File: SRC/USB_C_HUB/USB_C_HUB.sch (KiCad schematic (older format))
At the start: 38 parts

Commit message: PD controller_ power components inclusion pending
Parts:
- removed C? (x3): 10uF, symbol Device:C_Small
- removed C? (x2): 47uF, symbol Device:C_Small
- removed C?: 1uF, symbol Device:C_Small
- removed C?: 0.01uF, symbol Device:C_Small
- removed C? (x2): 22uF, symbol Device:C_Small
- removed C? (x2): 220pF, symbol Device:C_Small
- removed C? (x3): 0.1uF, symbol Device:C_Small
- removed D?: D_Schottky, symbol Device:D_Schottky
- removed D?: D12V0L1B2LP-7B, Diode_SMD:D_01005_0402Metric, symbol dk_TVS-Diodes:PGB1010603MR
- removed J?: USB_C_Receptacle, symbol Connector:USB_C_Receptacle
- removed Q? (x2): SI7997DP, symbol usb_hub:SI7997DP
- removed Q? (x2): MMBF2201NT1G, digikey-footprints:SOT-323, symbol dk_Transistors-FETs-MOSFETs-Single:2N7002P_215
- removed R?: 10K_603, symbol Device:R_US
- removed R?: 30K_603, symbol Device:R_US
- removed R?: 20K_603, symbol Device:R_US
- removed R?: 5K_805, symbol Device:R_US
- removed R?: 100K, symbol Device:R_US
- removed R? (x6): 10K, symbol Device:R_US
- removed R?: 576K, symbol Device:R_US
- removed R? (x2): 1K, symbol Device:R_US
- removed U?: TPS65987D, symbol usb_hub:TPS65987D
- removed U?: TLV1701AIDBVR, Package_TO_SOT_SMD:SOT-23-5, symbol Amplifier_Operational:TLV172IDCK
- removed Z?: BZT52C11-7-F, digikey-footprints:SOD-123, symbol dk_Diodes-Zener-Single:MMSZ5231B-7-F
- added P?: USB_C_Plug, symbol Connector:USB_C_Plug
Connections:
- net labels added: VCONN
- net labels removed: +3.3V, +5V, ADCIN1, ADCIN2, COMP_IN, COMP_OUT, C_CC2, GND_FET, LDO_3V3, POWER_IN(PP_EXT1), PP_EXT_CNTRL
- wire segments 198 -> 13
- no-connect marks 12 -> 0
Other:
- note added: "Connected to computer(host).\n"
- note added: "UPWARD FACING PORT(UFP)\n"
- note removed: "BP_WaitFor3V3_Internal mode\ndiv=0.25, SPI_POCI=1\nR1=30K, R2=10K."
- note removed: "CHARGER INPUT\nTYPE C\nRECEPTACLE"
- note removed: "GND_NMOS comes from the \ncomparator. When no power is \npressent the comparator connectes the \nPP_EXT_CNTRL pin to GND via NMOS"
- note removed: "PP_EXT_CNTRL turns on the mosfet via \na gate thus making the PP_EXT1 mosfet\ngate zero. turning on the mosfet and\n allowing current flow"
- note removed: "The TPS65987D requires firmware \nprogramming via a downloadable GUI tool.\nRecomendation: Since the system takes in a \ncharger we can configure it as a Source device\n(read:https://www.embedded.com/usb-type-c-and-power-delivery-101-ports-and-connections/) \nSecondly: we can configure it as a DRP device that can source(provide) or sink(receive) power. Its a source when the charging \nreceptacle 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"
- note removed: "UNUSED \nIN THE TYPE C \nCHARGING INPUT"
- note removed: "VOLTAGE COMPARATOR"
- note removed: "sets the I2C address\nDIV = R2/(R1+R2)\nR1=5K, R2=20K\nDIV=0.8, ADD=011b"

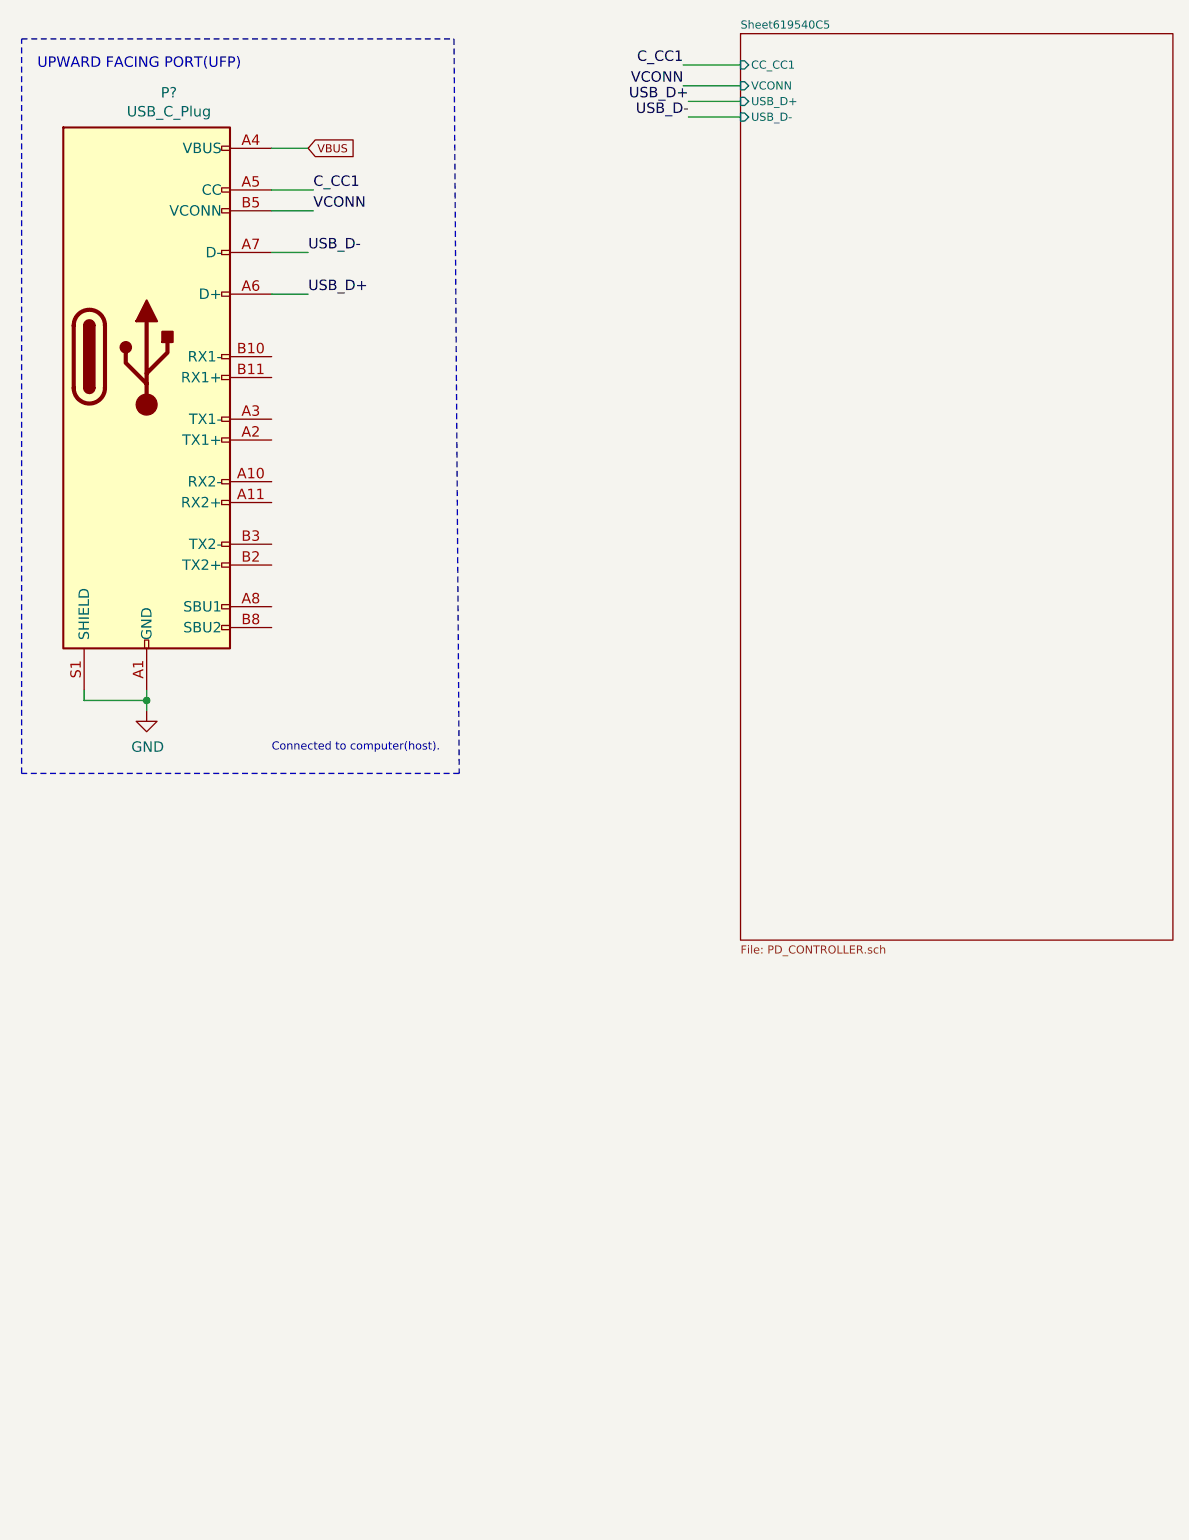
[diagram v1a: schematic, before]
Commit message: PD controller + variable voltage source input(will handle voltage requestvia PD)
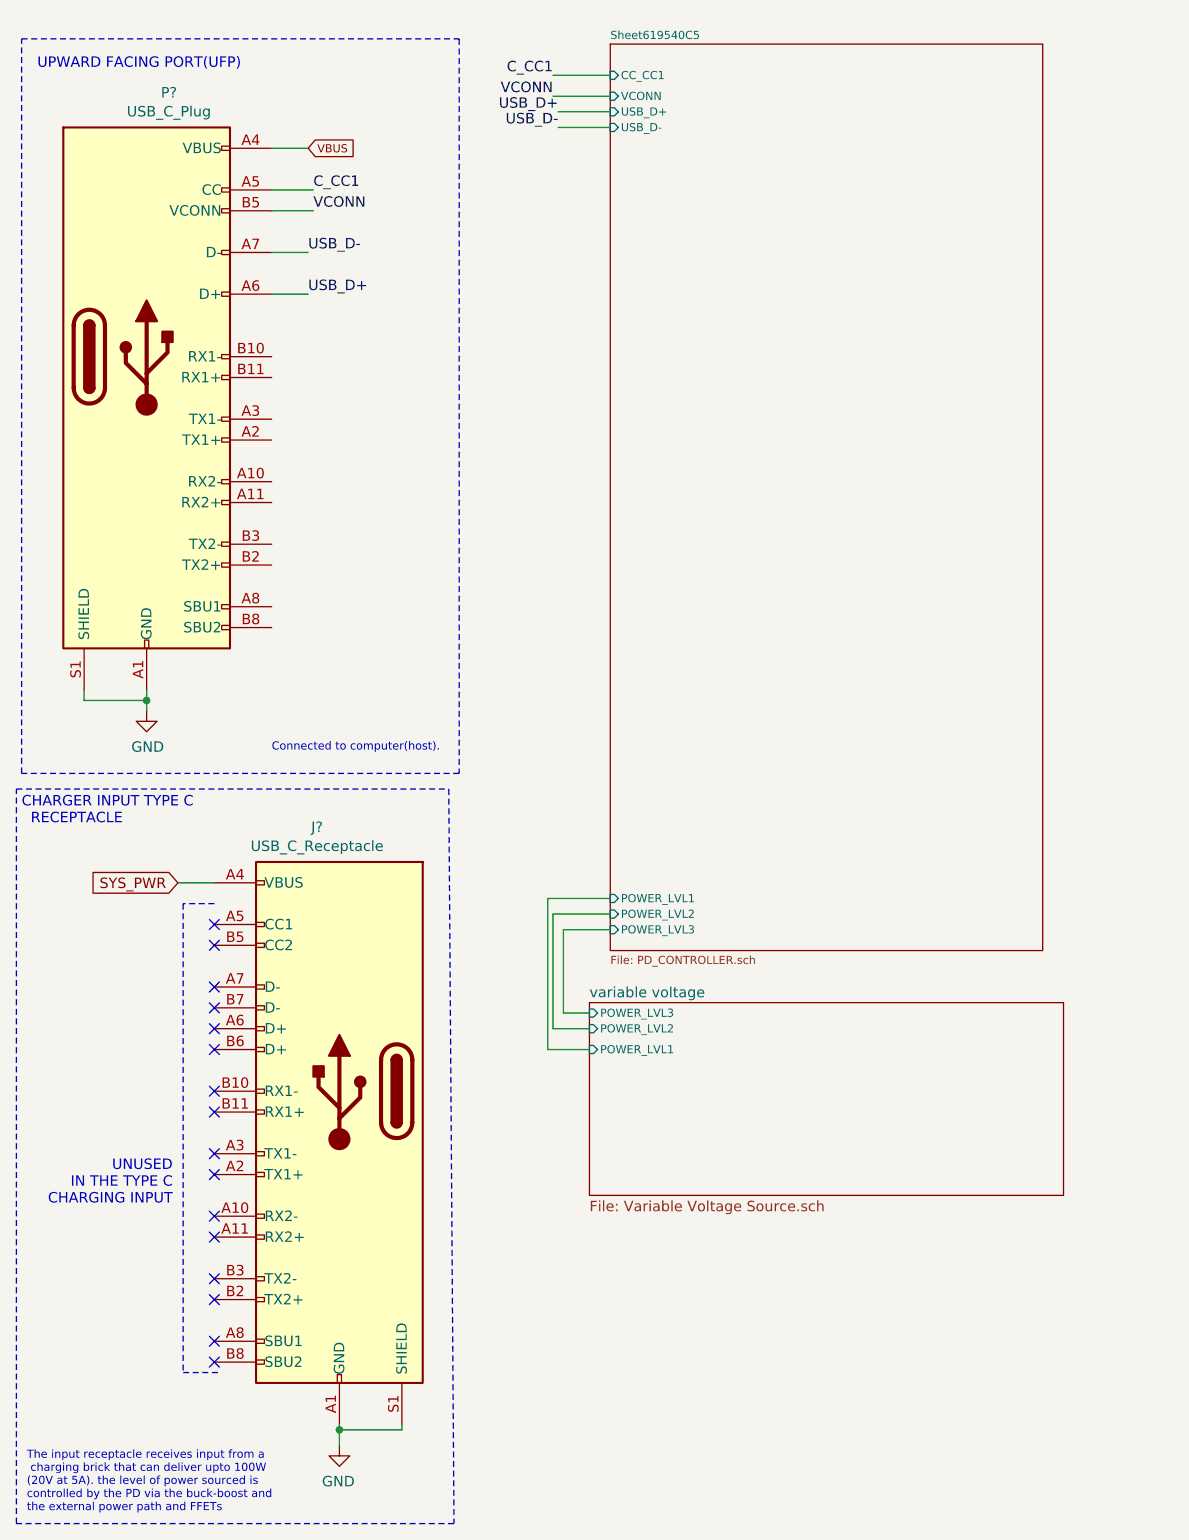
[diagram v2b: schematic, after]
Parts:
- added J?: USB_C_Receptacle, symbol Connector:USB_C_Receptacle
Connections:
- net GND: now also J?.A1 (GND), J?.A12 (GND), J?.B1 (GND), J?.B12 (GND), J?.S1 (SHIELD)
- new net SYS_PWR: J?.A4 (VBUS), J?.A9 (VBUS), J?.B4 (VBUS), J?.B9 (VBUS)
- no-connect marks 0 -> 16
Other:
- note added: "CHARGER INPUT TYPE C\n RECEPTACLE"
- note added: "The input receptacle receives input from a\n charging brick that can deliver upto 100W\n(20V at 5A). the level of power sourced is \ncontrolled by the PD via the buck-boost and \nthe external power path and FFETs"
- note added: "UNUSED \nIN THE TYPE C \nCHARGING INPUT"
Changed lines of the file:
@@
 $Descr A4 11693 8268
 encoding utf-8
-Sheet 1 2
+Sheet 1 3
 Title ""
 Date ""
@@
 	1750 1125 1925 1125
 Wire Notes Line
-	2625 600  2650 4125
+	2650 600  2650 4125
 Wire Notes Line
 	2650 4125 550  4125
@@
 	550  4125 550  600
 Wire Notes Line
-	550  600  2625 600
+	550  600  2650 600
 Wire Wire Line
 	1750 1825 1925 1825
@@
 Text GLabel 1925 1125 2    39   Input ~ 0
 VBUS
-Text Label 3725 725  2    50   ~ 0
+Text Label 3100 775  2    50   ~ 0
 C_CC1
-Text Label 3725 825  2    50   ~ 0
+Text Label 3100 875  2    50   ~ 0
 VCONN
 Wire Wire Line
-	3725 725  4000 725
-Wire Wire Line
-	3725 825  4000 825
-Text Label 3750 900  2    50   ~ 0
+	3100 775  3375 775
+Wire Wire Line
+	3100 875  3375 875
+Text Label 3125 950  2    50   ~ 0
 USB_D+
-Text Label 3750 975  2    50   ~ 0
+Text Label 3125 1025 2    50   ~ 0
 USB_D-
 $Sheet
-S 4000 575  2075 4350
+S 3375 625  2075 4350
 U 619540C6
 F0 "Sheet619540C5" 39
 F1 "PD_CONTROLLER.sch" 39
-F2 "CC_CC1" I L 4000 725 39
-F3 "VCONN" I L 4000 825 39
-F4 "USB_D+" I L 4000 900 39
-F5 "USB_D-" I L 4000 975 39
+F2 "CC_CC1" I L 3375 775 39
+F3 "VCONN" I L 3375 875 39
+F4 "USB_D+" I L 3375 950 39
+F5 "USB_D-" I L 3375 1025 39
+F6 "POWER_LVL1" I L 3375 4725 39
+F7 "POWER_LVL2" I L 3375 4800 39
+F8 "POWER_LVL3" I L 3375 4875 39
 $EndSheet
 Wire Wire Line
-	4000 900  3750 900
-Wire Wire Line
-	3750 975  4000 975
+	3375 950  3125 950
+Wire Wire Line
+	3125 1025 3375 1025
+Wire Notes Line
+	2600 4200 2625 7725
+Wire Wire Line
+	2075 7275 2075 7350
+Connection ~ 2075 7275
+Wire Wire Line
+	2375 7275 2075 7275
+Wire Wire Line
+	2375 7250 2375 7275
+NoConn ~ 1475 4950
+NoConn ~ 1475 4850
+Wire Notes Line
+	525  4200 2600 4200
+Wire Notes Line
+	525  7725 525  4200
+Wire Notes Line
+	2625 7725 525  7725
+Wire Wire Line
+	1475 4650 1300 4650
+Wire Wire Line
+	2075 7250 2075 7275
+$Comp
+L OLIMEX_Power:GND #PWR?
+U 1 1 61C31561
+P 2075 7350
+AR Path="/619540C6/61C31561" Ref="#PWR?"  Part="1"
+AR Path="/61C31561" Ref="#PWR?"  Part="1"
+F 0 "#PWR?" H 2075 7100 50  0001 C CNN
+F 1 "GND" H 2080 7177 50  0000 C CNN
+F 2 "" H 2075 7350 60  0000 C CNN
+F 3 "" H 2075 7350 60  0000 C CNN
+	1    2075 7350
+	-1   0    0    -1
+$EndComp
+Text Notes 1275 6200 2    50   ~ 0
+UNUSED \nIN THE TYPE C \nCHARGING INPUT
+Wire Notes Line
+	1325 7000 1500 7000
+Wire Notes Line
+	1325 4750 1325 7000
+Wire Notes Line
+	1475 4750 1325 4750
+NoConn ~ 1475 6950
+NoConn ~ 1475 6850
+NoConn ~ 1475 6650
+NoConn ~ 1475 6550
+NoConn ~ 1475 6350
+NoConn ~ 1475 6250
+NoConn ~ 1475 6050
+NoConn ~ 1475 5950
+NoConn ~ 1475 5750
+NoConn ~ 1475 5650
+Text Notes 550  4375 0    50   ~ 0
+CHARGER INPUT TYPE C\n  RECEPTACLE
+$Comp
+L Connector:USB_C_Receptacle J?
+U 1 1 61C31576
+P 2075 5650
+AR Path="/619540C6/61C31576" Ref="J?"  Part="1"
+AR Path="/61C31576" Ref="J?"  Part="1"
+F 0 "J?" H 2182 6917 50  0000 C CNN
+F 1 "USB_C_Receptacle" H 2182 6826 50  0000 C CNN
+F 2 "" H 2225 5650 50  0001 C CNN
+F 3 "https://www.usb.org/sites/default/files/documents/usb_type-c.zip" H 2225 5650 50  0001 C CNN
+	1    2075 5650
+	-1   0    0    -1
+$EndComp
+NoConn ~ 1475 5150
+NoConn ~ 1475 5250
+NoConn ~ 1475 5350
+NoConn ~ 1475 5450
+Text Notes 575  7675 0    39   ~ 0
+The input receptacle receives input from a\n charging brick that can deliver upto 100W\n(20V at 5A). the level of power sourced is \ncontrolled by the PD via the buck-boost and \nthe external power path and FFETs
+Text GLabel 1300 4650 0    50   Input ~ 0
+SYS_PWR
+$Sheet
+S 3275 5225 2275 925
+U 61C45066
+F0 "variable voltage" 50
+F1 "Variable Voltage Source.sch" 50
+F2 "POWER_LVL1" I L 3275 5450 39
+F3 "POWER_LVL2" I L 3275 5350 39
+F4 "POWER_LVL3" I L 3275 5275 39
+$EndSheet
+Wire Wire Line
+	3375 4725 3075 4725
+Wire Wire Line
+	3075 4725 3075 5450
+Wire Wire Line
+	3075 5450 3275 5450
+Wire Wire Line
+	3275 5350 3100 5350
+Wire Wire Line
+	3100 5350 3100 4800
+Wire Wire Line
+	3100 4800 3375 4800
+Wire Wire Line
+	3375 4875 3150 4875
+Wire Wire Line
+	3150 4875 3150 5275
+Wire Wire Line
+	3150 5275 3275 5275
 $EndSCHEMATC

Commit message: With ST PD controller(sink)100W
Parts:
- added D?: ESDA25P35, digikey-footprints:SOD-523, symbol dk_TVS-Diodes:ESD5Z3_3T1G
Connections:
- net CC1_PWR: now reaches J?.A5 (CC1)
- net CC2_PWR: now reaches J?.B5 (CC2)
- net SYS_PWR renamed PWR_IN
- no-connect marks 16 -> 14
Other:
- note added: "PRESERVED FOR USE LATER_\nNO CONNECTION TO THE SCHEMATIC"
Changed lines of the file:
@@
 Text GLabel 1925 1125 2    39   Input ~ 0
 VBUS
-Text Label 3100 775  2    50   ~ 0
-C_CC1
-Text Label 3100 875  2    50   ~ 0
-VCONN
-Wire Wire Line
-	3100 775  3375 775
-Wire Wire Line
-	3100 875  3375 875
-Text Label 3125 950  2    50   ~ 0
-USB_D+
-Text Label 3125 1025 2    50   ~ 0
-USB_D-
-$Sheet
-S 3375 625  2075 4350
-U 619540C6
-F0 "Sheet619540C5" 39
-F1 "PD_CONTROLLER.sch" 39
-F2 "CC_CC1" I L 3375 775 39
-F3 "VCONN" I L 3375 875 39
-F4 "USB_D+" I L 3375 950 39
-F5 "USB_D-" I L 3375 1025 39
-F6 "POWER_LVL1" I L 3375 4725 39
-F7 "POWER_LVL2" I L 3375 4800 39
-F8 "POWER_LVL3" I L 3375 4875 39
-$EndSheet
-Wire Wire Line
-	3375 950  3125 950
-Wire Wire Line
-	3125 1025 3375 1025
 Wire Notes Line
-	2600 4200 2625 7725
+	2650 4200 2650 7725
 Wire Wire Line
 	2075 7275 2075 7350
@@
 Wire Wire Line
 	2375 7250 2375 7275
-NoConn ~ 1475 4950
-NoConn ~ 1475 4850
 Wire Notes Line
-	525  4200 2600 4200
+	525  4200 2650 4200
 Wire Notes Line
 	525  7725 525  4200
 Wire Notes Line
-	2625 7725 525  7725
+	2650 7725 525  7725
 Wire Wire Line
 	1475 4650 1300 4650
@@
 	1325 7000 1500 7000
 Wire Notes Line
-	1325 4750 1325 7000
+	1325 5050 1325 7000
 Wire Notes Line
-	1475 4750 1325 4750
+	1525 5050 1325 5050
 NoConn ~ 1475 6950
 NoConn ~ 1475 6850
@@
 Text Notes 575  7675 0    39   ~ 0
 The input receptacle receives input from a\n charging brick that can deliver upto 100W\n(20V at 5A). the level of power sourced is \ncontrolled by the PD via the buck-boost and \nthe external power path and FFETs
-Text GLabel 1300 4650 0    50   Input ~ 0
-SYS_PWR
+Wire Wire Line
+	1475 4850 1300 4850
+Wire Wire Line
+	1475 4950 1300 4950
+Text Label 1300 4850 2    39   ~ 0
+CC1_PWR
+$Comp
+L dk_TVS-Diodes:ESD5Z3_3T1G D?
+U 1 1 61D69198
+P 1500 6900
+AR Path="/61C45066/61D69198" Ref="D?"  Part="1"
+AR Path="/61D69198" Ref="D?"  Part="1"
+F 0 "D?" V 1553 6772 60  0000 R CNN
+F 1 "ESDA25P35" V 1447 6772 60  0000 R CNN
+F 2 "digikey-footprints:SOD-523" H 1700 7100 60  0001 L CNN
+F 3 "https://www.onsemi.com/pub/Collateral/ESD5Z2.5T1-D.PDF" H 1700 7200 60  0001 L CNN
+F 4 "ESD5Z3.3T1GOSCT-ND" H 1700 7300 60  0001 L CNN "Digi-Key_PN"
+F 5 "ESD5Z3.3T1G" H 1700 7400 60  0001 L CNN "MPN"
+F 6 "Circuit Protection" H 1700 7500 60  0001 L CNN "Category"
+F 7 "TVS - Diodes" H 1700 7600 60  0001 L CNN "Family"
+F 8 "https://www.onsemi.com/pub/Collateral/ESD5Z2.5T1-D.PDF" H 1700 7700 60  0001 L CNN "DK_Datasheet_Link"
+F 9 "/product-detail/en/on-semiconductor/ESD5Z3.3T1G/ESD5Z3.3T1GOSCT-ND/1967044" H 1700 7800 60  0001 L CNN "DK_Detail_Page"
+F 10 "TVS DIODE 3.3V 14.1V SOD523" H 1700 7900 60  0001 L CNN "Description"
+F 11 "ON Semiconductor" H 1700 8000 60  0001 L CNN "Manufacturer"
+F 12 "Active" H 1700 8100 60  0001 L CNN "Status"
+	1    1500 6900
+	0    -1   -1   0
+$EndComp
+Text Label 1300 4950 2    39   ~ 0
+CC2_PWR
+Text Label 1300 4650 2    50   ~ 0
+PWR_IN
+Text Label 2950 4525 2    50   ~ 0
+PWR_IN
 $Sheet
-S 3275 5225 2275 925
-U 61C45066
-F0 "variable voltage" 50
-F1 "Variable Voltage Source.sch" 50
-F2 "POWER_LVL1" I L 3275 5450 39
-F3 "POWER_LVL2" I L 3275 5350 39
-F4 "POWER_LVL3" I L 3275 5275 39
+S 11775 6725 2525 1500
+U 61EF7DEC
+F0 "UFP_PD_CONTROLLER" 50
+F1 "UFP_PD_CTRL + VAR_V_SOURCE.sch" 50
 $EndSheet
+Text Notes 12150 7325 0    50   ~ 0
+PRESERVED FOR USE LATER_\nNO CONNECTION TO THE SCHEMATIC
 Wire Wire Line
-	3375 4725 3075 4725
-Wire Wire Line
-	3075 4725 3075 5450
-Wire Wire Line
-	3075 5450 3275 5450
-Wire Wire Line
-	3275 5350 3100 5350
-Wire Wire Line
-	3100 5350 3100 4800
-Wire Wire Line
-	3100 4800 3375 4800
-Wire Wire Line
-	3375 4875 3150 4875
-Wire Wire Line
-	3150 4875 3150 5275
-Wire Wire Line
-	3150 5275 3275 5275
+	3050 4525 2950 4525
+$Sheet
+S 3050 4425 2325 975
+U 61DDBD9F
+F0 "ST_PD CHARGING" 39
+F1 "ST_PD CHARGING CONTROLLER.sch" 39
+F2 "PWR_IN" I L 3050 4525 39
+$EndSheet
 $EndSCHEMATC

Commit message: With ST PD controller(sink)100W
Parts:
- removed D?: ESDA25P35, digikey-footprints:SOD-523, symbol dk_TVS-Diodes:ESD5Z3_3T1G
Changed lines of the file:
@@
 $Descr A4 11693 8268
 encoding utf-8
-Sheet 1 3
+Sheet 1 4
 Title ""
 Date ""
@@
 Text Label 1300 4850 2    39   ~ 0
 CC1_PWR
-$Comp
-L dk_TVS-Diodes:ESD5Z3_3T1G D?
-U 1 1 61D69198
-P 1500 6900
-AR Path="/61C45066/61D69198" Ref="D?"  Part="1"
-AR Path="/61D69198" Ref="D?"  Part="1"
-F 0 "D?" V 1553 6772 60  0000 R CNN
-F 1 "ESDA25P35" V 1447 6772 60  0000 R CNN
-F 2 "digikey-footprints:SOD-523" H 1700 7100 60  0001 L CNN
-F 3 "https://www.onsemi.com/pub/Collateral/ESD5Z2.5T1-D.PDF" H 1700 7200 60  0001 L CNN
-F 4 "ESD5Z3.3T1GOSCT-ND" H 1700 7300 60  0001 L CNN "Digi-Key_PN"
-F 5 "ESD5Z3.3T1G" H 1700 7400 60  0001 L CNN "MPN"
-F 6 "Circuit Protection" H 1700 7500 60  0001 L CNN "Category"
-F 7 "TVS - Diodes" H 1700 7600 60  0001 L CNN "Family"
-F 8 "https://www.onsemi.com/pub/Collateral/ESD5Z2.5T1-D.PDF" H 1700 7700 60  0001 L CNN "DK_Datasheet_Link"
-F 9 "/product-detail/en/on-semiconductor/ESD5Z3.3T1G/ESD5Z3.3T1GOSCT-ND/1967044" H 1700 7800 60  0001 L CNN "DK_Detail_Page"
-F 10 "TVS DIODE 3.3V 14.1V SOD523" H 1700 7900 60  0001 L CNN "Description"
-F 11 "ON Semiconductor" H 1700 8000 60  0001 L CNN "Manufacturer"
-F 12 "Active" H 1700 8100 60  0001 L CNN "Status"
-	1    1500 6900
-	0    -1   -1   0
-$EndComp
 Text Label 1300 4950 2    39   ~ 0
 CC2_PWR
@@
 F2 "PWR_IN" I L 3050 4525 39
 $EndSheet
+$Sheet
+S 3175 700  1675 1050
+U 61F5E4BA
+F0 "5V_BUCK" 50
+F1 "5V_BUCK.sch" 50
+$EndSheet
 $EndSCHEMATC

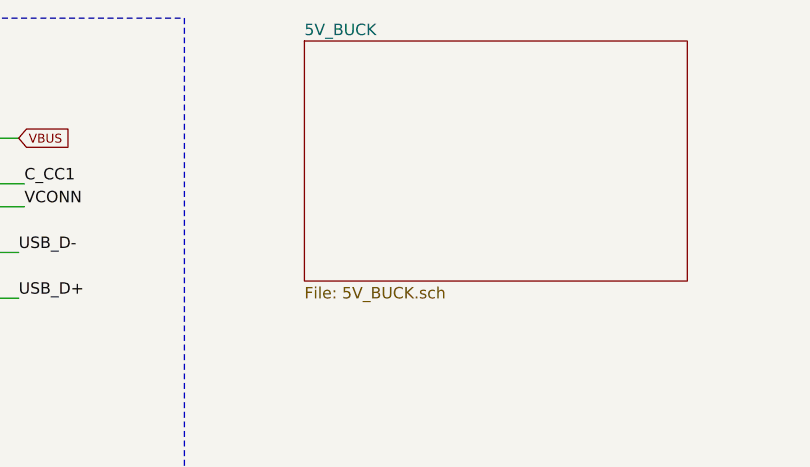
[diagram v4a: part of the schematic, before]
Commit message: With ST_PD controller, Buck $ Boost regulators
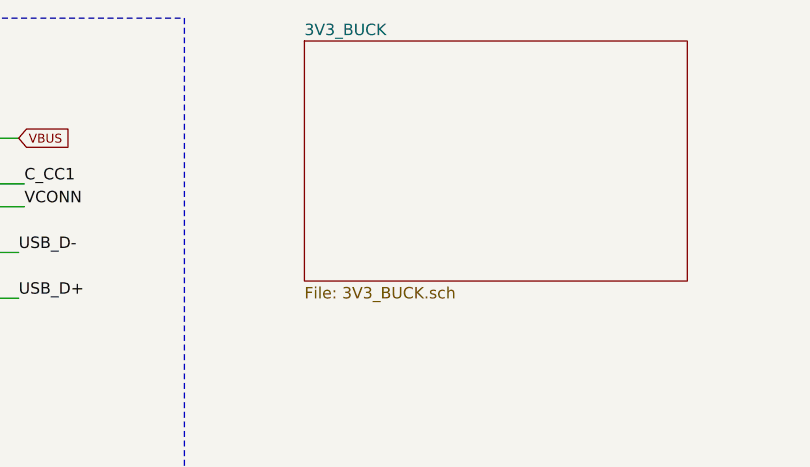
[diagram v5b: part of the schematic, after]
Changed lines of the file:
@@
 S 3175 700  1675 1050
 U 61F5E4BA
-F0 "5V_BUCK" 50
-F1 "5V_BUCK.sch" 50
+F0 "3V3_BUCK" 50
+F1 "3V3_BUCK.sch" 50
 $EndSheet
 $EndSCHEMATC
